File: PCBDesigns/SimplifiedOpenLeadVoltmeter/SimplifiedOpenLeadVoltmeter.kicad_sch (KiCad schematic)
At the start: 36 parts, among them J14 Barrel_Jack, J2 Conn_01x03_Pin, J3 Conn_01x04_MountingPin, J5 Conn_01x03_Pin, Q8 AO3400A MOSFET, SW3 SW_SPDT, U1 ADuM1200AR, U10 LM4040DBZ-2.5, U13 ISO1540, U14 RFM-0505S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

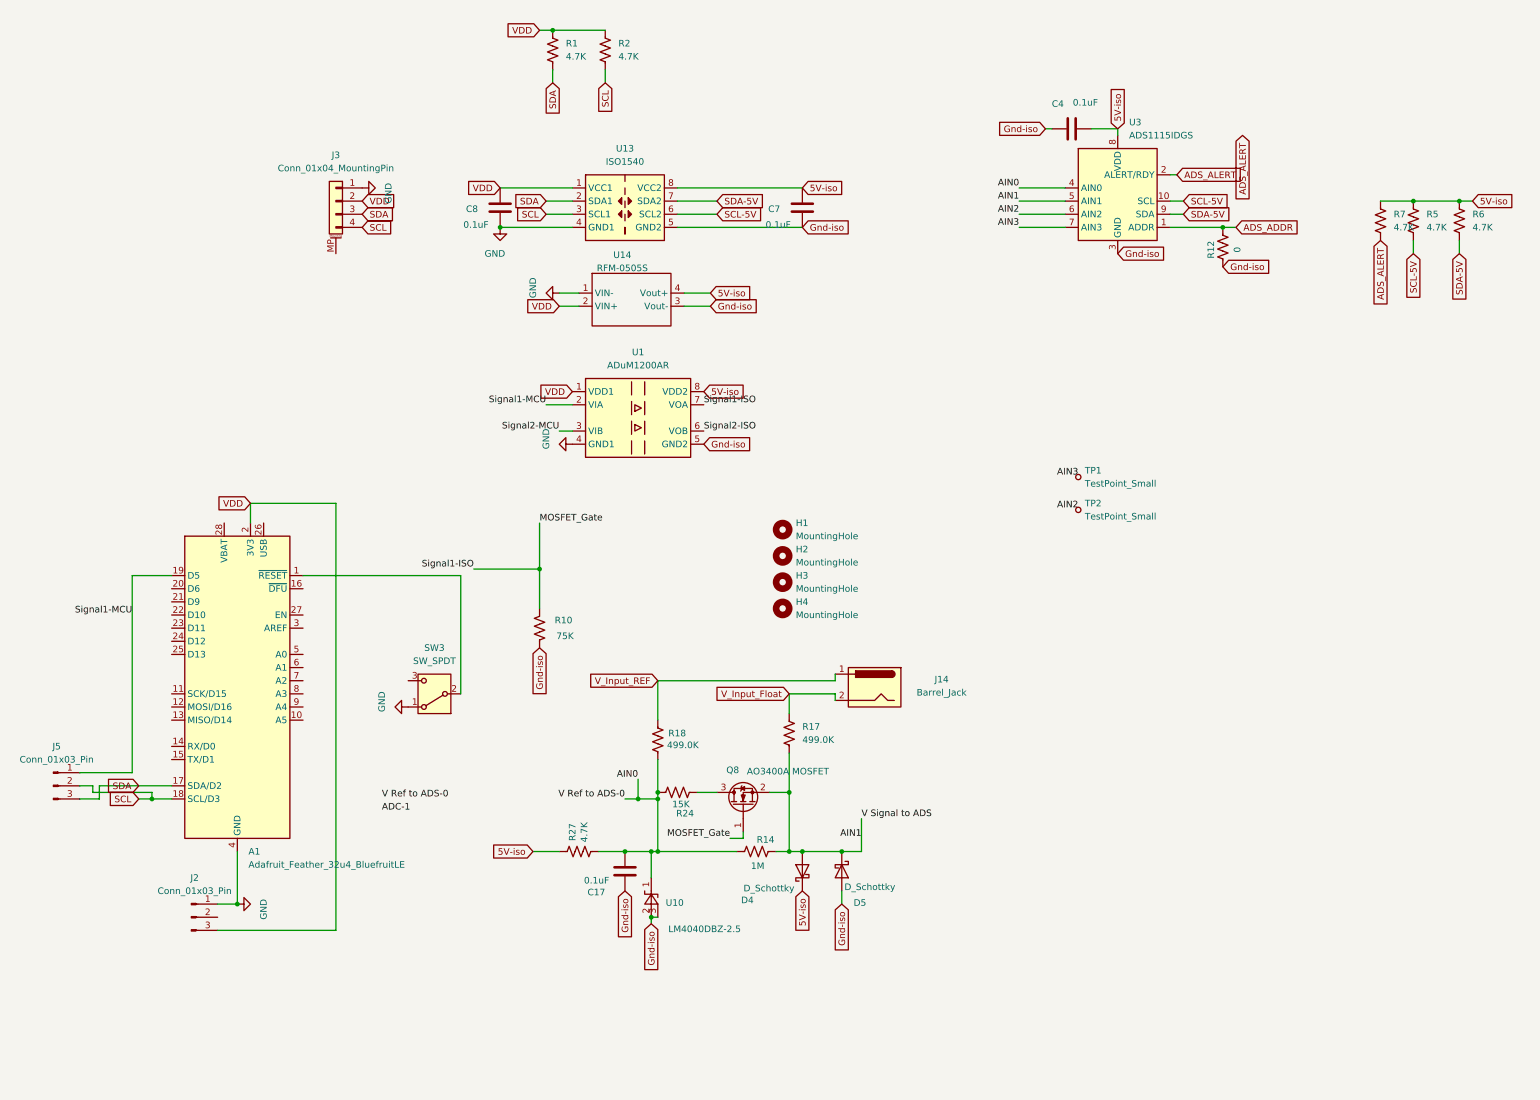
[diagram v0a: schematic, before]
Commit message: Updates, see description
Updated programming for open lead detect board
worked on various PCBs, including a new open lead voltmeter design with few components
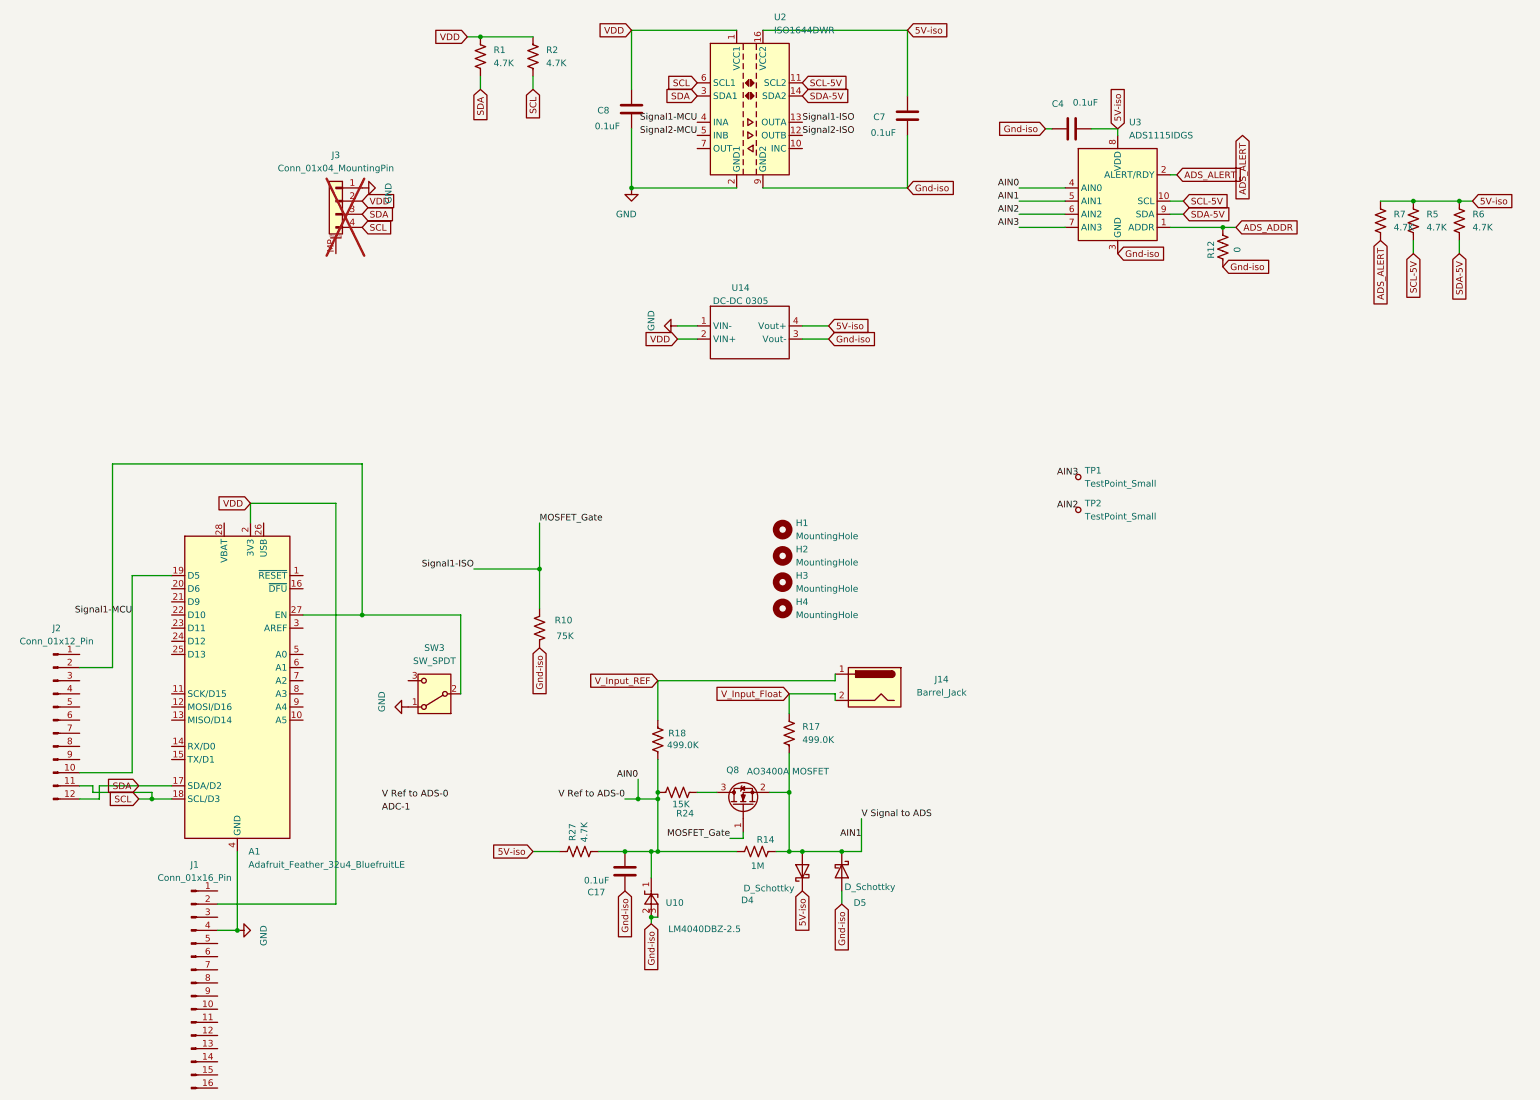
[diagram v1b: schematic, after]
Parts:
- removed J2, J5: Conn_01x03_Pin, Connector_PinHeader_2.54mm:PinHeader_1x03_P2.54mm_Vertical, symbol Connector:Conn_01x03_Pin
- removed U1: ADuM1200AR, Package_SO:SOIC-8_3.9x4.9mm_P1.27mm, symbol Isolator:ADuM1200AR
- removed U13: ISO1540, Package_SO:SOIC-8_3.9x4.9mm_P1.27mm, symbol Isolator:ISO1540
- added J1: Conn_01x16_Pin, Connector_PinSocket_2.54mm:PinSocket_1x16_P2.54mm_Vertical, symbol Connector:Conn_01x16_Pin
- added J2: Conn_01x12_Pin, Connector_PinSocket_2.54mm:PinSocket_1x12_P2.54mm_Vertical, symbol Connector:Conn_01x12_Pin
- added U2: ISO1644DWR, Package_SO:SOIC-16W_7.5x10.3mm_P1.27mm, symbol Isolator:ISO1644DWR
- C17, C4, C7, C8: footprint Capacitor_SMD:C_0805_2012Metric_Pad1.18x1.45mm_HandSolder -> Capacitor_SMD:C_0603_1608Metric_Pad1.08x0.95mm_HandSolder
- J3: now not fitted
- R1, R10, R2, R27, R5, R6, R7: footprint Resistor_SMD:R_0805_2012Metric_Pad1.20x1.40mm_HandSolder -> Resistor_SMD:R_0603_1608Metric_Pad0.98x0.95mm_HandSolder
- U14: value RFM-0505S -> DC-DC 0305
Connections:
- net 5V-iso: now also U2.16 (VCC2)
- net GND: now also J1.4 (Pin_4), U2.2 (GND1), U2.8 (GND1)
- net Gnd-iso: now also U2.15 (GND2), U2.9 (GND2)
- net MOSFET_Gate: now also U2.13 (OUTA)
- net SCL: now also J2.11 (Pin_11), U2.6 (SCL1)
- net SCL-5V: now also U2.11 (SCL2)
- net SDA: now also J2.12 (Pin_12), U2.3 (SDA1)
- net SDA-5V: now also U2.14 (SDA2)
- net Signal1-MCU: now also J2.10 (Pin_10), U2.4 (INA)
- net Signal2-ISO: now also U2.12 (OUTB)
- net Signal2-MCU: now also U2.5 (INB)
- net VDD: now also J1.2 (Pin_2), U2.1 (VCC1)
- net at SW3.2 (B): now also A1.27 (EN), J2.2 (Pin_2); no longer A1.1 (~{RESET})
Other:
- moved on the sheet: C7, C8, R1, R2, U14

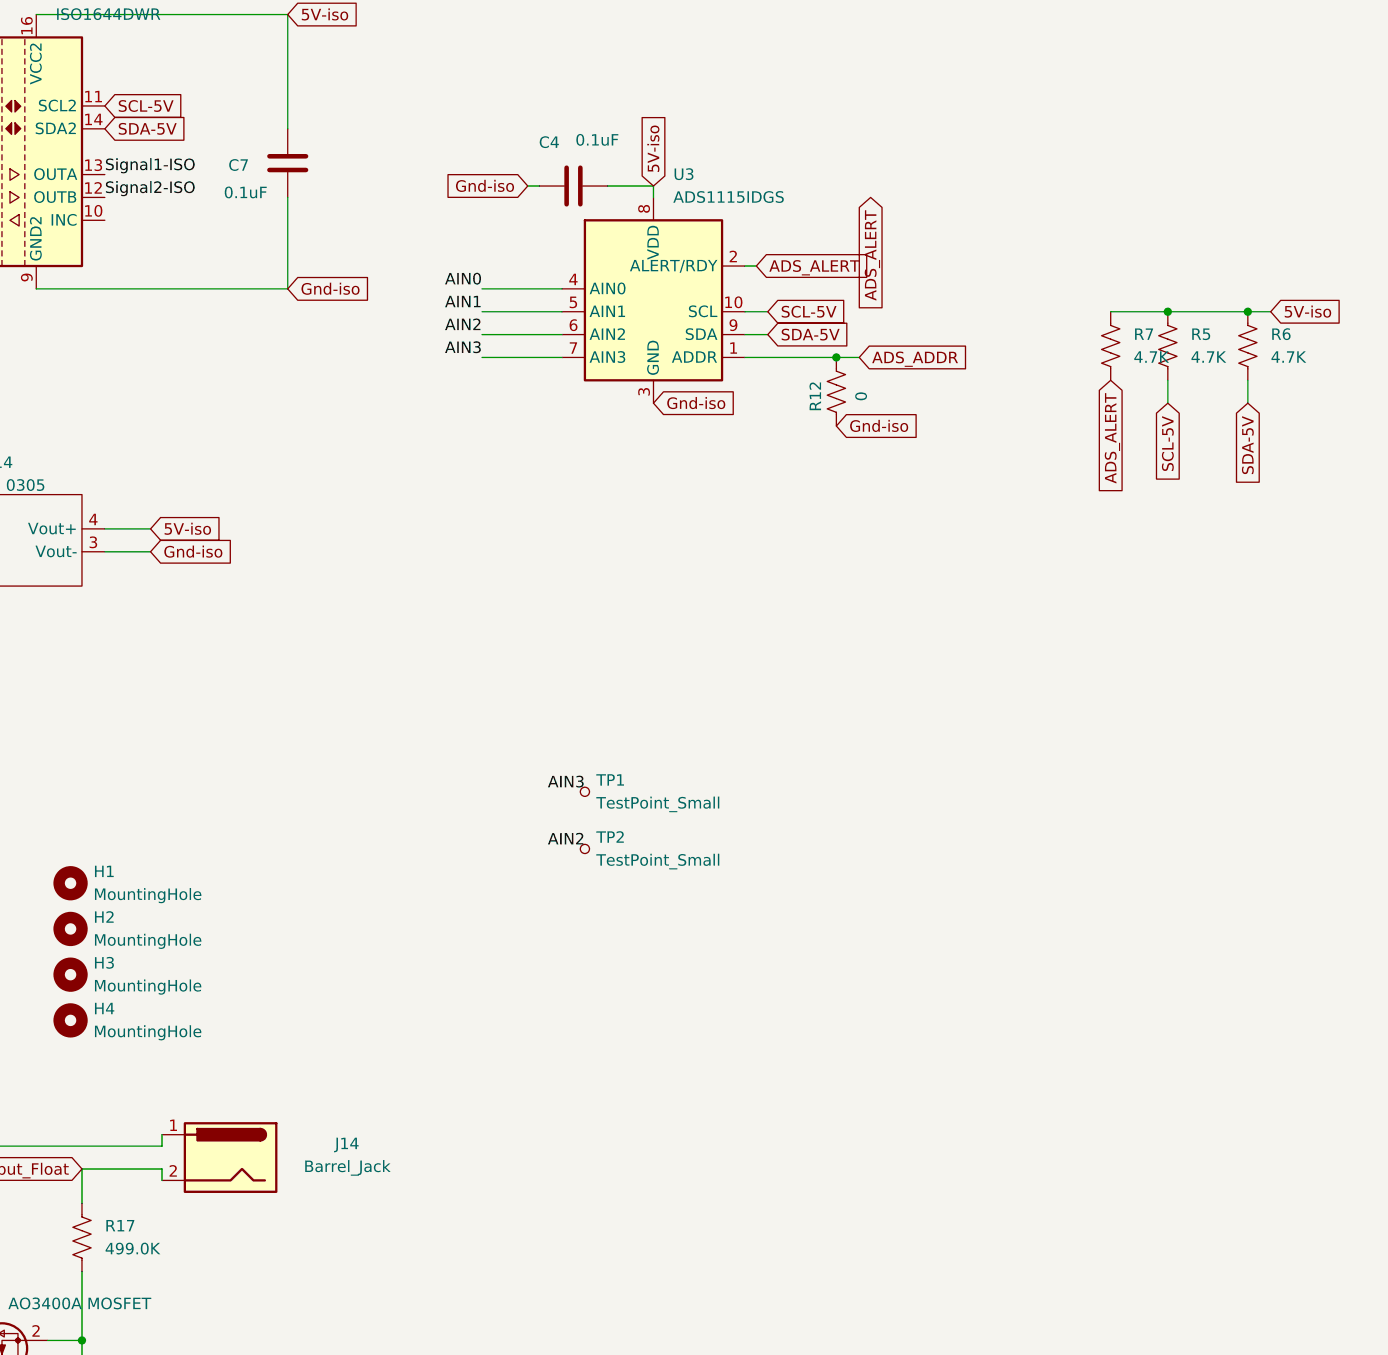
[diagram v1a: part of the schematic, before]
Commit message: Made circuit boards and BLE circuit boards.
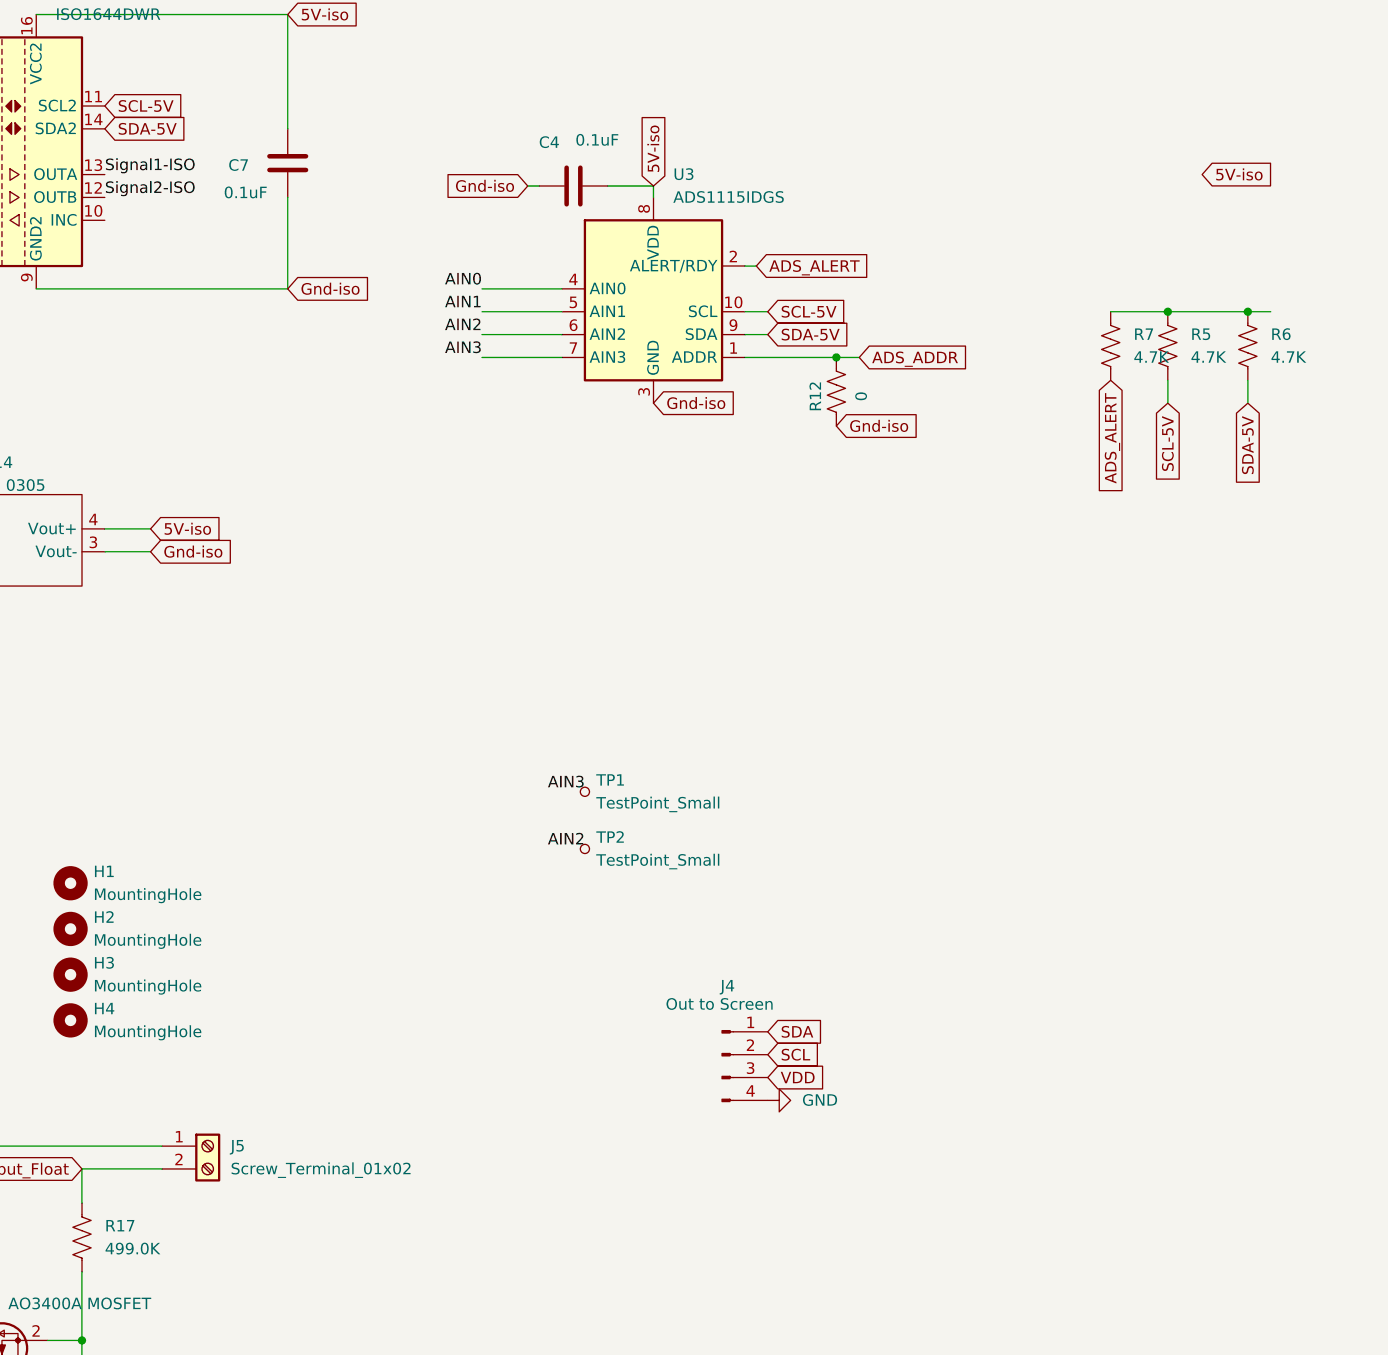
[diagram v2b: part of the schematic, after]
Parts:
- removed J14: Barrel_Jack, Connector_BarrelJack:BarrelJack_Horizontal, symbol Connector:Barrel_Jack
- added J4: Out to Screen, Connector_PinSocket_2.54mm:PinSocket_1x04_P2.54mm_Vertical, symbol Connector:Conn_01x04_Pin
- added J5: Screw_Terminal_01x02, TerminalBlock_CUI:TerminalBlock_CUI_TB007-508-02_1x02_P5.08mm_Horizontal, symbol Connector:Screw_Terminal_01x02
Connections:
- net 5V-iso: no longer R5.1, R6.1, R7.1
- net GND: now also J4.4 (Pin_4)
- net SCL: now also J4.2 (Pin_2)
- net SDA: now also J4.1 (Pin_1)
- net VDD: now also J4.3 (Pin_3)
- net V_Input_Float: now also J5.2 (Pin_2)
- net V_Input_REF: now also J5.1 (Pin_1)
- new net: R5.1, R6.1, R7.1
